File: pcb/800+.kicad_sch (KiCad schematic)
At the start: 22 parts, among them J1 2inch LCD, J2 USB_B_Micro, J4 Cradle, J5 Battery, J6 Conn_01x18, Q1 S8050, Q2 AO3401A

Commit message: alpha2 pcb
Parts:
- removed J6: Conn_01x18, 880+:ESP_TestPad, symbol Connector_Generic:Conn_01x18
- added C10, C9: 10u, Capacitor_SMD:C_0805_2012Metric, symbol Device:C
- added C9: 1u, Capacitor_SMD:C_0805_2012Metric, symbol Device:C
- added F1: Polyfuse, Resistor_SMD:R_1210_3225Metric_Pad1.30x2.65mm_HandSolder, symbol Device:Polyfuse
- added J6: ESP_JTAG, Connector_PinHeader_2.54mm:PinHeader_1x06_P2.54mm_Vertical, symbol Connector:Conn_01x06_Socket
- added J7: ESP_PROG, Connector_PinHeader_2.54mm:PinHeader_1x06_P2.54mm_Vertical, symbol Connector:Conn_01x06_Socket
- added R7: 1M, Resistor_SMD:R_0805_2012Metric, symbol Device:R
- added R8, R9: 10k, Resistor_SMD:R_0805_2012Metric, symbol Device:R
- added TP1: TestPoint, TestPoint:TestPoint_THTPad_D2.5mm_Drill1.2mm, symbol Connector:TestPoint
- added U2: USBLC6, Package_TO_SOT_SMD:SOT-23-6, symbol Random_SRAM_Parts:USBLC6_Fixed
- added U2: ESP32-S3-WROOM-1U, PCM_Espressif:ESP32-S3-WROOM-1, symbol PCM_Espressif:ESP32-S3-WROOM-1
- added U4: AP1117, Package_TO_SOT_SMD:SOT-223, symbol regul:AP1117
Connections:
- net GND: now also J2.5 (GND), C10.2, C9.1, C9.2, J6.2 (Pin_2), J7.2 (Pin_2), R7.2, U2.1 (GND), U2.2 (GND), U2.22 (GPIO14/TOUCH14/ADC2_CH3/FSPIWP/FSPIDQS/SUBSPIWP), U2.23 (GPIO21), U2.24 (GPIO47/SPICLK_P/SUBSPICLK_P_DIFF), U2.25 (GPIO48/SPICLK_N/SUBSPICLK_N_DIFF), U2.38 (GPIO2/TOUCH2/ADC1_CH1), U2.40 (GND), U2.41 (GND), U2.8 (GPIO15/U0RTS/ADC2_CH4/XTAL_32K_P), U2.9 (GPIO16/U0CTS/ADC2_CH5/XTAL_32K_N), U4.1 (GND/ADJ)
- net LCD_BLC: now also U2.39 (GPIO1/TOUCH1/ADC1_CH0)
- net LCD_CLK: now also U2.19 (GPIO11/TOUCH11/ADC2_CH0/FSPID/FSPIIO5/SUBSPID)
- net LCD_CS: now also U2.20 (GPIO12/TOUCH12/ADC2_CH1/FSPICLK/FSPIIO6/SUBSPICLK)
- net LCD_DIN: now also U2.18 (GPIO10/TOUCH10/ADC1_CH9/FSPICS0/FSPIIO4/SUBSPICS0)
- net LCD_D/C: now also U2.21 (GPIO13/TOUCH13/ADC2_CH2/FSPIQ/FSPIIO7/SUBSPIQ)
- net LCD_RESET: now also U2.17 (GPIO9/TOUCH9/ADC1_CH8/FSPIHD/SUBSPIHD)
- net LED_Drive: now also U2.31 (GPIO38/FSPIWP/SUBSPIWP)
- net LED_TP: now also Q2.3 (D); no longer Q2.2 (S)
- net MSP_P1.3: now also U2.6 (GPIO6/TOUCH6/ADC1_CH5)
- net MSP_P1.4: now also U2.5 (GPIO5/TOUCH5/ADC1_CH4)
- net MSP_P1.5: now also U2.4 (GPIO4/TOUCH4/ADC1_CH3)
- net MSP_P1.6: now also U2.7 (GPIO7/TOUCH7/ADC1_CH6)
- net MSP_P1.7: now also U2.12 (GPIO8/TOUCH8/ADC1_CH7/SUBSPICS1)
- net at J2.1 (VBUS): now also F1.2, TP1.1, U2.5 (Vbus)
- net DN: now reaches J2.2 (D-)
- net DN: now also U2.1 (I/O2)
- net DP: now reaches J2.3 (D+)
- net DP: now also U2.3 (I/O1)
- net at J2.6 (Shield): now also R7.1
- net +3V3 renamed +3.3V
- net +3.3V: now also Q2.2 (S), C10.1, J6.1 (Pin_1), J7.1 (Pin_1), R8.2, R9.2, U2.2 (3V3), U4.2 (VO), U4.4 (VO); no longer Q2.3 (D)
- new net +5V: C9.1, F1.1, U4.3 (VI)
- new net D+: U2.14 (GPIO20/U1CTS/ADC2_CH9/CLK_OUT1/USB_D+), U2.4 (I/O1)
- new net D-: U2.13 (GPIO19/U1RTS/ADC2_CH8/CLK_OUT2/USB_D-), U2.6 (I/O2)
- new net ESP_EN: C9.2, J7.6 (Pin_6), R9.1, U2.3 (EN)
- new net ESP_IO0: J7.3 (Pin_3), R8.1, U2.27 (GPIO0/BOOT)
- new net ESP_RXD: J7.4 (Pin_4), U2.36 (U0RXD/GPIO44/CLK_OUT2)
- new net ESP_TO_MSP: U2.10 (GPIO17/U1TXD/ADC2_CH6)
- new net ESP_TXD: J7.5 (Pin_5), U2.37 (U0TXD/GPIO43/CLK_OUT1)
- new net MSP_TO_ESP: U2.11 (GPIO18/U1RXD/ADC2_CH7/CLK_OUT3)
- new net TCK: J6.3 (Pin_3), U2.32 (MTCK/GPIO39/CLK_OUT3/SUBSPICS1)
- new net TDI: J6.5 (Pin_5), U2.34 (MTDI/GPIO41/CLK_OUT1)
- new net TDO: J6.4 (Pin_4), U2.33 (MTDO/GPIO40/CLK_OUT2)
- new net TMS: J6.6 (Pin_6), U2.35 (MTMS/GPIO42)
- no-connect marks 1 -> 7
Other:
- note added: "NC are unused pins that don't have any usage restrictions"
- moved on the sheet: J4, J5, Q2, R5, R6

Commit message: current working kikad
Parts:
- R1: footprint Resistor_SMD:R_0805_2012Metric -> Resistor_SMD:R_1210_3225Metric
- R6: value R -> 10
- U2: value USBLC6 -> USBLC6-2
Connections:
- net +3.3V: no longer R3.1
- net GND: now also R3.1
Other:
- note added: "ESP32-S3-WROOM-1U-N16R8 16 MB (Quad SPI) 8 MB (Octal PSRAM)"
- note added: "Holes by D32 can get removed. Looks like they were for tagConnect like adapter Battery spring contacts have some pegs on bottom. Need holes added to footprint More bypass capacitors"
- note added: "TODO"
- moved on the sheet: J4, J5

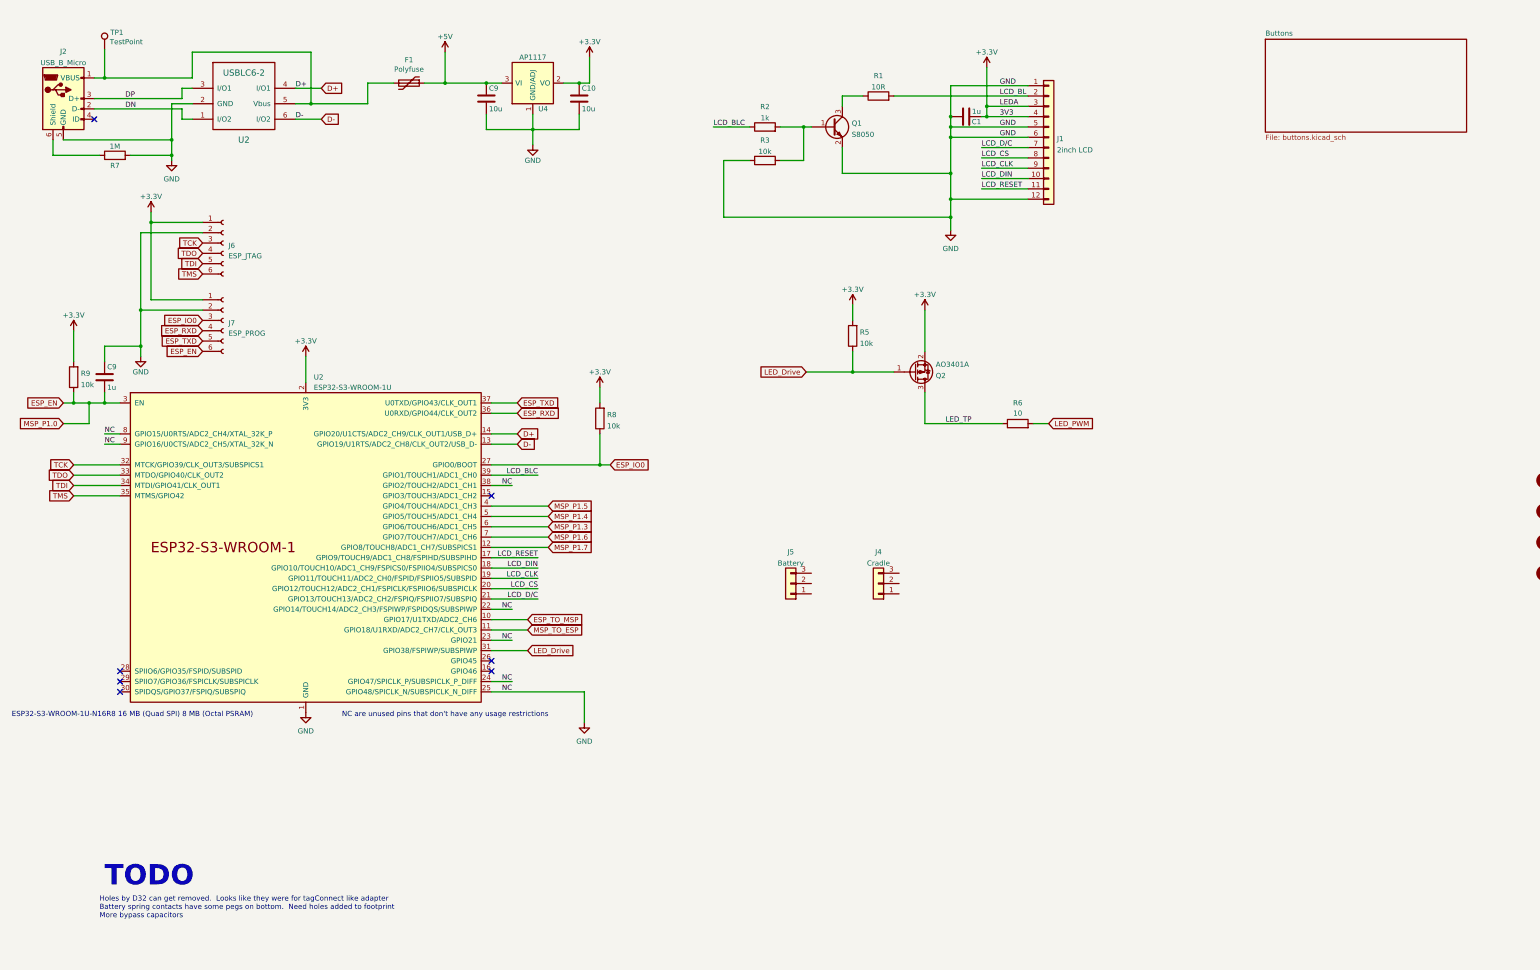
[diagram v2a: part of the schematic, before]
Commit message: add power to schematic
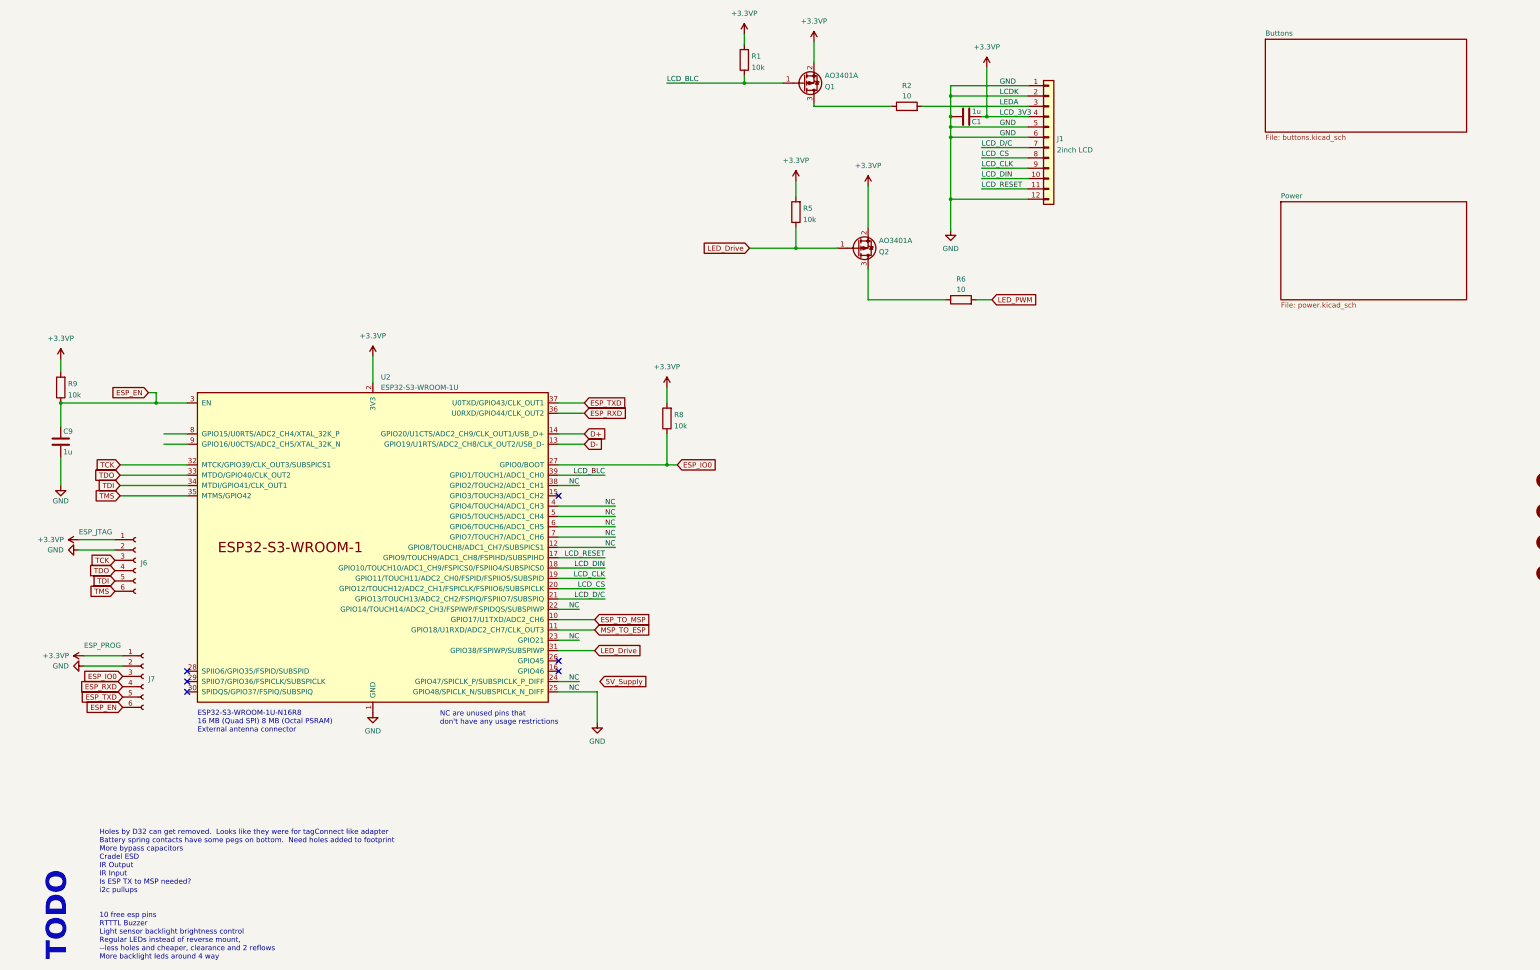
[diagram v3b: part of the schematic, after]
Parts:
- removed C10, C9: 10u, Capacitor_SMD:C_0805_2012Metric, symbol Device:C
- removed F1: Polyfuse, Resistor_SMD:R_1210_3225Metric_Pad1.30x2.65mm_HandSolder, symbol Device:Polyfuse
- removed J2: USB_B_Micro, Connector_USB:USB_Mini-B_Wuerth_65100516121_Horizontal, symbol Connector:USB_B_Micro
- removed J4: Cradle, Connector_JST:JST_GH_BM03B-GHS-TBT_1x03-1MP_P1.25mm_Vertical, symbol Connector_Generic:Conn_01x03
- removed J5: Battery, 880+:Battery_reuse, symbol Connector_Generic:Conn_01x03
- removed Q1: S8050, Package_TO_SOT_SMD:SOT-23, symbol Device:Q_NPN_BEC
- removed R3: 10k, Resistor_SMD:R_0805_2012Metric, symbol Device:R
- removed R7: 1M, Resistor_SMD:R_0805_2012Metric, symbol Device:R
- removed TP1: TestPoint, TestPoint:TestPoint_THTPad_D2.5mm_Drill1.2mm, symbol Connector:TestPoint
- removed U2: USBLC6-2, Package_TO_SOT_SMD:SOT-23-6, symbol Random_SRAM_Parts:USBLC6_Fixed
- removed U4: AP1117, Package_TO_SOT_SMD:SOT-223, symbol regul:AP1117
- added Q1: AO3401A, Package_TO_SOT_SMD:SOT-23, symbol Transistor_FET:AO3401A
- R1: value 10R -> 10k; footprint Resistor_SMD:R_1210_3225Metric -> Resistor_SMD:R_0805_2012Metric
- R2: value 1k -> 10; footprint Resistor_SMD:R_0805_2012Metric -> Resistor_SMD:R_1210_3225Metric
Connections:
- net MSP_P1.3 is gone; now on net GND: U2.6 (GPIO6/TOUCH6/ADC1_CH5)
- net MSP_P1.4 is gone; now on net GND: U2.5 (GPIO5/TOUCH5/ADC1_CH4)
- net MSP_P1.5 is gone; now on net GND: U2.4 (GPIO4/TOUCH4/ADC1_CH3)
- net MSP_P1.6 is gone; now on net GND: U2.7 (GPIO7/TOUCH7/ADC1_CH6)
- net MSP_P1.7 is gone; now on net GND: U2.12 (GPIO8/TOUCH8/ADC1_CH7/SUBSPICS1)
- net ESP_EN: now also C9.1; no longer C9.2
- net GND: now also C9.2, J1.2 (Pin_2); no longer C9.1, U2.8 (GPIO15/U0RTS/ADC2_CH4/XTAL_32K_P), U2.9 (GPIO16/U0CTS/ADC2_CH5/XTAL_32K_N)
- net LCD_BLC: now also R1.1, Q1.1 (G); no longer R2.1
- net LEDA: now reaches R2.2
- net LEDA: now also J1.3 (Pin_3)
- net +3.3V renamed +3.3VP
- net +3.3VP: now also R1.2, Q1.2 (S); no longer J1.3 (Pin_3)
- removed net LCD_BL: J1.2 (Pin_2), R1.2
- net LED_TP: no longer names the net of Q2.3 (D), R6.1
- new net: Q1.3 (D), R2.1
- no-connect marks 7 -> 6
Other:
- added sheet Power (power.kicad_sch)
- note added: "ESP32-S3-WROOM-1U-N16R8 16 MB (Quad SPI) 8 MB (Octal PSRAM) External antenna connector"
- note added: "Holes by D32 can get removed. Looks like they were for tagConnect like adapter Battery spring contacts have some pegs on bottom. Need holes added to footprint More bypass capacitors Cradel ESD IR Output IR Input Is ESP TX to MSP needed? i2c pullups 10 free esp pins RTTTL Buzzer Light sensor backlight brightness control Regular LEDs instead of reverse mount, --less holes and cheaper, clearance and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"
- note removed: "ESP32-S3-WROOM-1U-N16R8 16 MB (Quad SPI) 8 MB (Octal PSRAM)"
- note removed: "Holes by D32 can get removed. Looks like they were for tagConnect like adapter Battery spring contacts have some pegs on bottom. Need holes added to footprint More bypass capacitors"
- moved on the sheet: C9, J6, J7, Q2, R5, R6, R8, R9, U2

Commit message: more schematic updates
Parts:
- added BZ1: Buzzer, symbol Device:Buzzer
- added D33, D34: LED, 880+:IR_led, symbol Device:LED
- added Q3, Q4: AO3401A, Package_TO_SOT_SMD:SOT-23, symbol Transistor_FET:AO3401A
- added R10, R18: 10k, Resistor_SMD:R_0805_2012Metric, symbol Device:R
- added R14, R15: 22, Resistor_SMD:R_1210_3225Metric, symbol Device:R
- added U7: TSOP75340TT, 880+:IR_input, symbol 880+:TSOP75340TT
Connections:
- net +3.3VP: now also Q3.2 (S), Q4.2 (S), R10.2, R18.2, U7.2 (Vs)
- net 5V_Supply: now also U2.24 (GPIO47/SPICLK_P/SUBSPICLK_P_DIFF)
- net ESP_TO_MSP: no longer U2.10 (GPIO17/U1TXD/ADC2_CH6)
- net GND: now also BZ1.2 (-), D33.1 (K), D34.1 (K), U7.1 (GND); no longer U2.23 (GPIO21), U2.24 (GPIO47/SPICLK_P/SUBSPICLK_P_DIFF), U2.38 (GPIO2/TOUCH2/ADC1_CH1), U2.4 (GPIO4/TOUCH4/ADC1_CH3)
- new net: D33.2 (A), R14.2
- new net: Q3.3 (D), R14.1, R15.1
- new net: D34.2 (A), R15.2
- new net: BZ1.1 (+), Q4.3 (D)
- new net Buzzer_output: Q4.1 (G), R18.1, U2.4 (GPIO4/TOUCH4/ADC1_CH3)
- new net IR_input: U2.23 (GPIO21), U7.3 (OUT)
- new net IR_output: Q3.1 (G), R10.1, U2.38 (GPIO2/TOUCH2/ADC1_CH1)
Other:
- note added: "1.5V 100mA"
- note added: "Holes by D32 can get removed. Looks like they were for tagConnect like adapter Battery spring contacts have some pegs on bottom. Need holes added to footprint Aliexpress 2.5mm x 5p connector maybe same size??? More bypass capacitors Cradel pinout Is ESP TX to MSP needed? Removed it, we will see.... Rolling ball might work as last switch on button matrix RTTTL Buzzer 5020 footprint Light sensor ba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"
- note removed: "Holes by D32 can get removed. Looks like they were for tagConnect like adapter Battery spring contacts have some pegs on bottom. Need holes added to footprint More bypass capacitors Cradel ESD IR Output IR Input Is ESP TX to MSP needed? i2c pullups 10 free esp pins RTTTL Buzzer Light sensor backlight brightness control Regular LEDs instead of reverse mount, --less holes and cheaper, clearance and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"

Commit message: ready to route????
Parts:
- removed H2, H3: Programming JTAG, MountingHole:MountingHole_3mm, symbol Mechanical:MountingHole
- added R19, R20: 4.7k, Resistor_SMD:R_0805_2012Metric, symbol Device:R
- added R21: 0, Resistor_SMD:R_1206_3216Metric, symbol Device:R
- added U12: VEML7700-TR, 880+:VEML7700, symbol 880+:VEML7700-TT
- BZ1: value Buzzer -> 5020 Passive; footprint (none) -> 880+:5020passiveBuzzer
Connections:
- net +3.3VP: now also R19.2, R20.1, U12.2 (VDD)
- net GND: now also R21.1, U12.3 (GND); no longer BZ1.2 (-)
- net LightSensor_SDA: now reaches U2.8 (GPIO15/U0RTS/ADC2_CH4/XTAL_32K_P)
- net LightSensor_SDA: now also R19.1, U12.4 (SDA)
- net LightSensor_SCL: now reaches U2.9 (GPIO16/U0CTS/ADC2_CH5/XTAL_32K_N)
- net LightSensor_SCL: now also R20.2, U12.1 (SCL)
- new net: BZ1.2 (-), R21.2
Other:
- note added: "ESP32 6 free GPIO MSP430 0 free gpio Battery spring contacts have some pegs on bottom. Need holes added to footprint Aliexpress 2.5mm x 5p connector maybe same size??? More bypass capacitors Cradel pinout Is ESP TX to MSP needed? Removed it, we will see.... Rolling ball might work as last switch on button matrix Regular LEDs instead of reverse mount, --less holes and cheaper, clearance and 2 refl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"
- note removed: "Holes by D32 can get removed. Looks like they were for tagConnect like adapter Battery spring contacts have some pegs on bottom. Need holes added to footprint Aliexpress 2.5mm x 5p connector maybe same size??? More bypass capacitors Cradel pinout Is ESP TX to MSP needed? Removed it, we will see.... Rolling ball might work as last switch on button matrix RTTTL Buzzer 5020 footprint Light sensor ba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"
